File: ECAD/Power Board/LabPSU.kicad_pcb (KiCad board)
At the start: 2 copper layers, 74 parts, among them J1 DC-IN, J2 CTRL, J3 UPDI, J4 +, J5 -, Q1 Si7148DP, Q2 Si7148DP, U1 LM2594HVN-5.0, U2 LM5118MH, U3 LM358, U4 ATtiny414-SS, U5 MCP4811, U6 INA180A3

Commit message: v1 routed
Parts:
- Q1, Q2: value Si7148DP -> Si7454FDP
- R1: value 90K -> 100K
- R9: value 80K -> 82K
- moved TP2 40.9 mm to (65.5, 98.3)
- moved C27 38.7 mm to (110.4, 137.4)
- moved H3 38.7 mm to (110.4, 142.7)
- moved C28 21.7 mm to (58.8, 137.3)
- moved H4 21.7 mm to (58.8, 142.6)
- moved J5 17.3 mm to (95.8, 137.9)
- moved J4 11.0 mm to (124.7, 137.9)
- moved TP10 7.38 mm to (131.3, 121.4)
- moved TP1 5.73 mm to (62.2, 83.3)
- moved TP4 3.61 mm to (78.7, 99.8)
- moved C26 1.85 mm to (130.9, 62.6)
- moved H2 1.85 mm to (130.9, 57.1)
- moved C2 0.76 mm to (70.4, 94.5)
- moved C3 0.51 mm to (70.4, 91.9)
- moved C5 0.25 mm to (70.4, 89.4)
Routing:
- net EN: track 7.84 -> 39.6 mm, vias 1 -> 3
- net +5V: track 102.3 -> 127.8 mm, vias 2 -> 4
- net GND: track 36.7 -> 55.3 mm, vias 38 -> 64
- net VBUS: track 66.1 -> 78.5 mm
- net IOUT: track 29.2 -> 32.8 mm
- net Net-(C17-Pad1): vias 0 -> 30
- net Net-(C14-Pad2): vias 0 -> 30
- added copper zone on B.Cu, net Net-(C14-Pad2)
- added copper zone on B.Cu, net Net-(C17-Pad1)
- added copper zone on F.Cu, net VOUT
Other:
- board outline added: 82.8 x 95.5 mm
- board text added: "Buck-Boost Board"

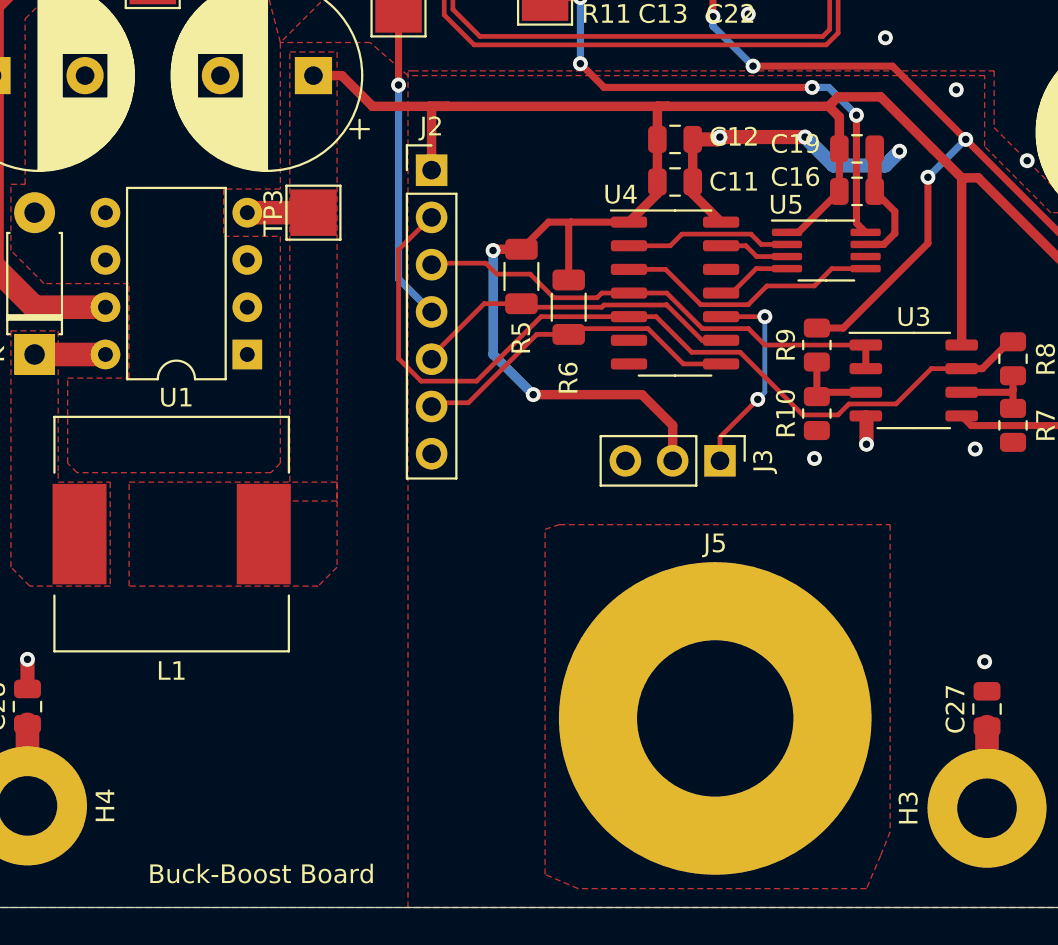
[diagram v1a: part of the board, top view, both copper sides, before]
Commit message: SOIC instead of MSOP
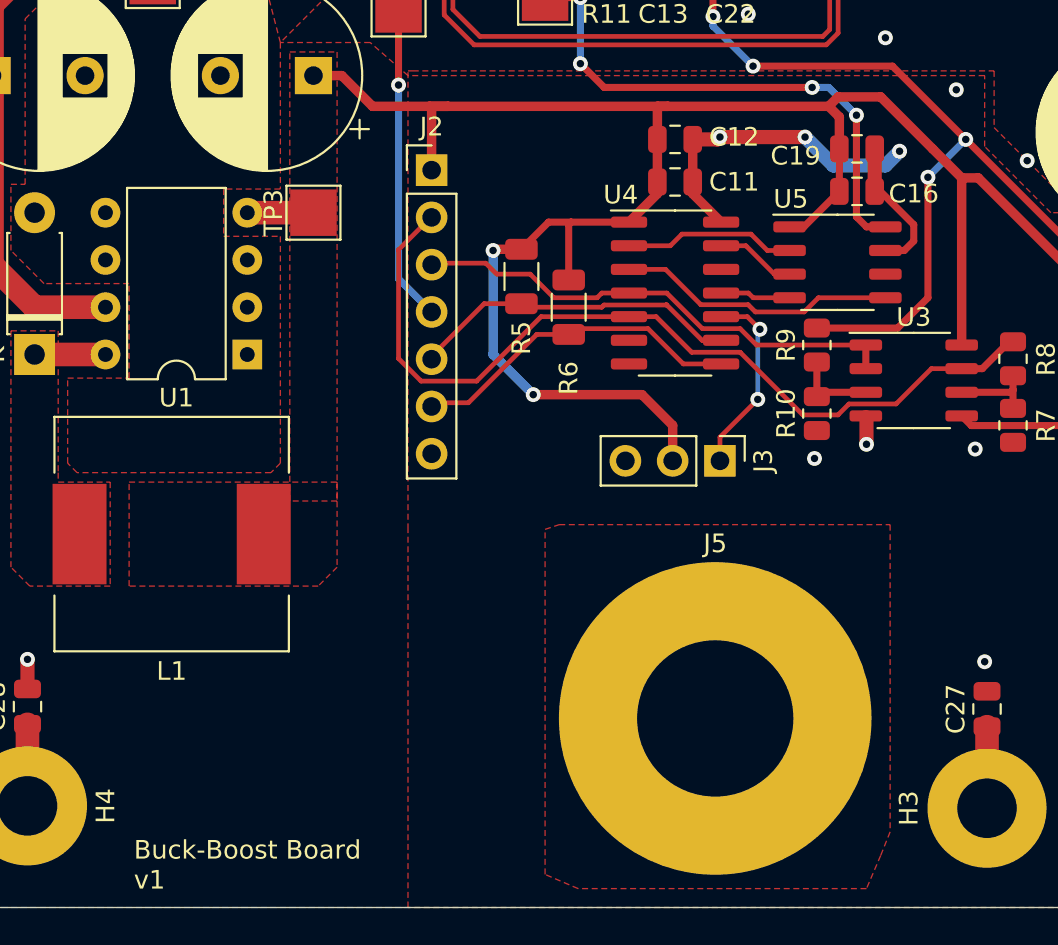
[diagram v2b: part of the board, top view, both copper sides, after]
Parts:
- U5: footprint Package_SO:MSOP-8_3x3mm_P0.65mm -> Package_SO:SO-8_3.9x4.9mm_P1.27mm
- moved U5 0.87 mm to (102.3, 113.4)
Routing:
- net VOUT: track 57.6 -> 59.3 mm
- net GND: track 55.3 -> 56.3 mm
- net /UPDI: track 11.1 -> 10.3 mm
- net /FB: track 35.9 -> 36.7 mm
- net /LDAC: track 14.3 -> 15.0 mm
- net /SCK: track 3.78 -> 4.31 mm
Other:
- board text added: "Buck-Boost Board v1"
- board text removed: "Buck-Boost Board"

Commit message: ina286
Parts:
- U6: value INA180A3 -> INA286; footprint Package_TO_SOT_SMD:SOT-23-5 -> Package_SO:SO-8_3.9x4.9mm_P1.27mm
- moved TP10 15.6 mm to (115.7, 120.5)
- moved C25 3.54 mm to (133.6, 116.1), turned to 270 degrees
- moved U6 2.54 mm to (129.9, 116.0), turned to 90 degrees
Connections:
- U6 pad 1: IOUT -> VOUT
- U6 pad 3: Net-(C17-Pad1) -> GND
- U6 pad 4: VOUT -> (no net)
- U6 pad 5: +5V -> IOUT
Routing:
- net +5V: track 127.6 -> 143.2 mm
- net IOUT: track 32.8 -> 27.2 mm
- net Net-(C17-Pad1): track 3.01 -> 5.44 mm
- net VOUT: track 59.3 -> 61.4 mm
- net GND: track 56.3 -> 54.4 mm, vias 64 -> 67

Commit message: Update LabPSU.kicad_pcb
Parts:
- moved J5 10.0 mm to (85.8, 137.9)
